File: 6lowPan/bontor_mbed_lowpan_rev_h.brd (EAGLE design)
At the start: 99.6 x 107 mm, 172 parts, among them IC1 SIM900, IC2 74HC595D, IC3 74HC595D, IC4 ADE7758RW, IC5 74HC595D, U2 W5500, X1 NX2520SA

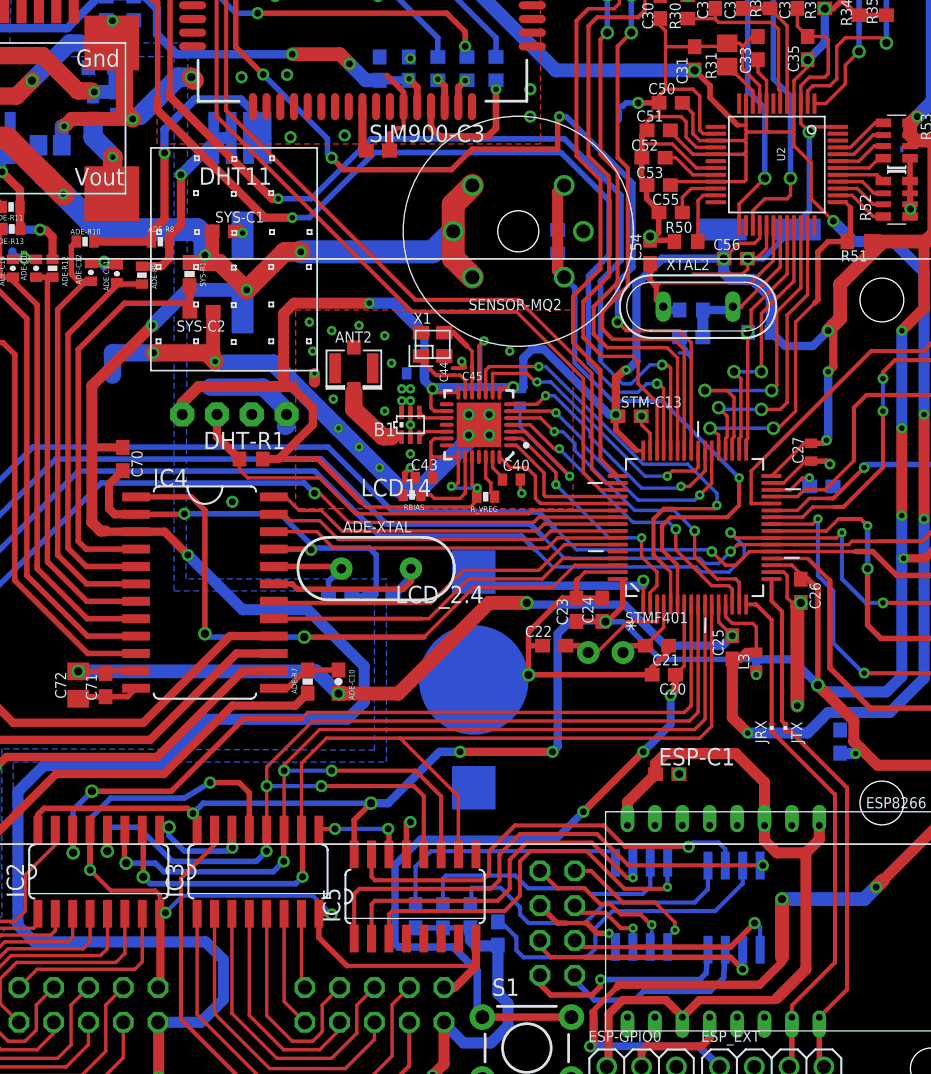
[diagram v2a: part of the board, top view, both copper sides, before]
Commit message: added on off button and remove LCD resstor
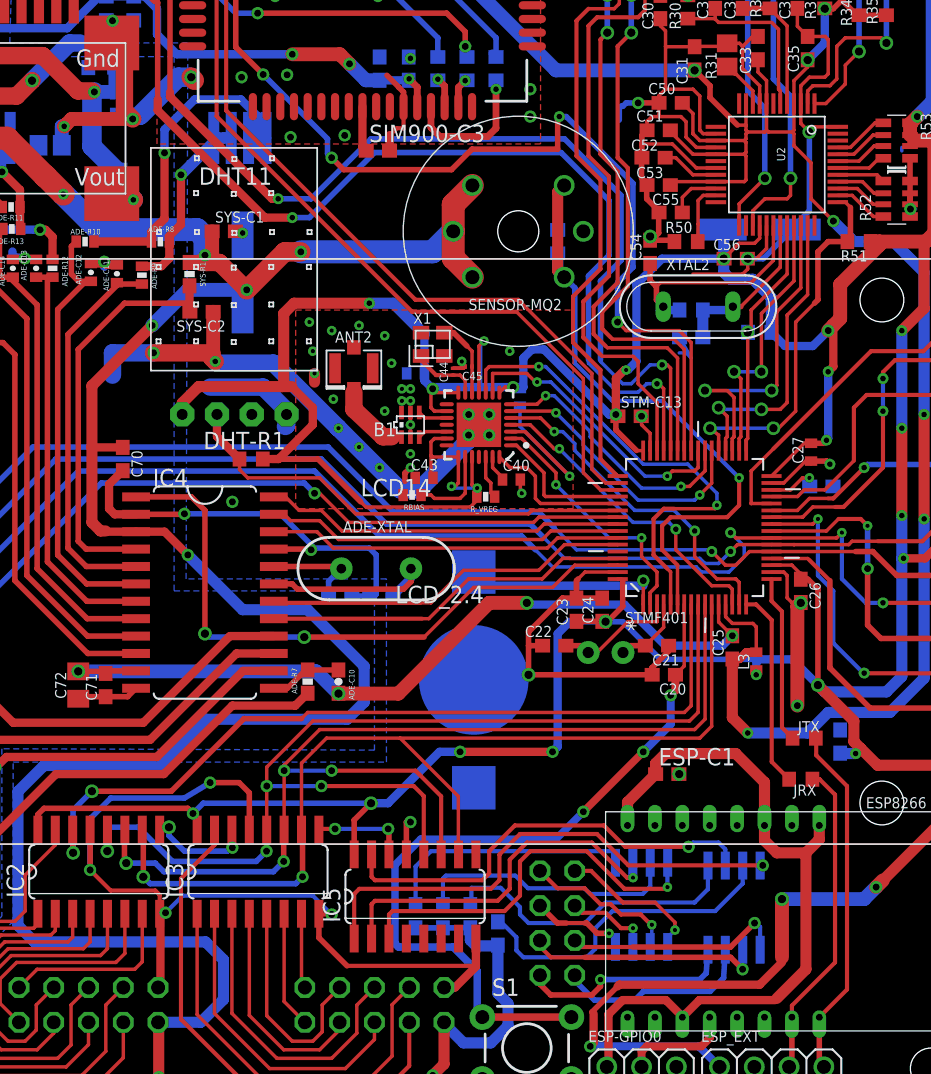
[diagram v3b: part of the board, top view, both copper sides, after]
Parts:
- JRX, JTX: device rcl:R0201 -> rcl:R0603
- PWR: device rcl:R0402 -> rcl:R0805
- moved PWR 5.89 mm to (37.3, 66.8)
- moved JRX 4.31 mm to (87.2, 23.4), turned to 180 degrees
- moved JTX 1.57 mm to (87.5, 26.4), turned to 180 degrees
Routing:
- net VDD: track 578.3 -> 584.9 mm
- net N$71: track 9.96 -> 14.5 mm
- net ESP_RX: track 27.8 -> 23.4 mm
- net DC_VOUT: track 6.23 -> 3.97 mm
- net ESP_TX: track 27.6 -> 25.9 mm
- net N$72: track 11.0 -> 12.3 mm
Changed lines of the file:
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@@
 <attribute name="VALUE" x="80.33" y="86.675" size="1.27" layer="27" rot="R180"/>
 </element>
-<element name="PWR" library="rcl" package="R0402" value="" x="35.5875" y="72.4125" smashed="yes" rot="MR270">
-<attribute name="NAME" x="36.1725" y="71.2025" size="0.6096" layer="26" rot="MR90"/>
-<attribute name="VALUE" x="37.4925" y="73.0475" size="1.27" layer="28" rot="MR270"/>
+<element name="PWR" library="rcl" package="R0805" value="" x="37.3375" y="66.7875" smashed="yes" rot="MR270">
+<attribute name="NAME" x="37.9225" y="65.5775" size="0.6096" layer="26" rot="MR90"/>
+<attribute name="VALUE" x="39.2425" y="67.4225" size="1.27" layer="28" rot="MR270"/>
 </element>
 <element name="S1" library="SparkFun-Electromechanical" package="TACTILE-PTH" value="" x="67.25" y="3.75"/>
@@
 <attribute name="VALUE" x="69.46" y="98.0975" size="1.27" layer="27" font="vector" ratio="10" rot="R270"/>
 </element>
-<element name="JRX" library="rcl" package="R0201" value="0" x="85.125" y="27.125" smashed="yes" rot="R90">
-<attribute name="NAME" x="84.74" y="25.99" size="0.8128" layer="25" rot="R90"/>
-<attribute name="VALUE" x="87.03" y="26.49" size="1.27" layer="27" rot="R90"/>
-</element>
-<element name="JTX" library="rcl" package="R0201" value="0" x="86.125" y="27.125" smashed="yes" rot="R90">
-<attribute name="NAME" x="87.365" y="25.99" size="0.8128" layer="25" rot="R90"/>
-<attribute name="VALUE" x="88.03" y="26.49" size="1.27" layer="27" rot="R90"/>
+<element name="JRX" library="rcl" package="R0603" value="0" x="87.25" y="23.375" smashed="yes" rot="R180">
+<attribute name="NAME" x="88.385" y="22.99" size="0.8128" layer="25" rot="R180"/>
+<attribute name="VALUE" x="87.885" y="25.28" size="1.27" layer="27" rot="R180"/>
+</element>
+<element name="JTX" library="rcl" package="R0603" value="0" x="87.5" y="26.375" smashed="yes" rot="R180">
+<attribute name="NAME" x="88.635" y="27.615" size="0.8128" layer="25" rot="R180"/>
+<attribute name="VALUE" x="88.135" y="28.28" size="1.27" layer="27" rot="R180"/>
 </element>
 <element name="ANT1" library="SparkFun" package="U.FL" value="U.FL" x="56.125" y="103.5" smashed="yes" rot="R270"/>
@@
 <wire x1="43.2125" y1="99.375" x2="41.825" y2="99.375" width="1.4224" layer="1"/>
 <contactref element="U$17" pad="VCC"/>
-<wire x1="35.5875" y1="73.0625" x2="35.5375" y2="73.1125" width="0.6096" layer="16"/>
 <wire x1="37.3125" y1="73.55" x2="35.675" y2="73.55" width="1.016" layer="16"/>
 <wire x1="31.9" y1="76.2" x2="27" y2="76.2" width="1.27" layer="1"/>
@@
 <via x="94.75" y="39.5" extent="1-16" drill="0.4"/>
 <wire x1="94.75" y1="39.5" x2="94.625" y2="39.5" width="0.6096" layer="16"/>
+<wire x1="37.3375" y1="67.7375" x2="35.5" y2="69.575" width="1.4224" layer="16"/>
+<wire x1="35.5" y1="69.575" x2="35.5" y2="73.375" width="1.4224" layer="16"/>
+<wire x1="35.5" y1="73.375" x2="35.675" y2="73.55" width="1.4224" layer="16"/>
 </signal>
 <signal name="SWD_NRST">
@@
 <wire x1="86.395" y1="2.375" x2="86.6" y2="2.58" width="0.4064" layer="1"/>
 <wire x1="86.6" y1="2.58" x2="86.6" y2="6" width="0.4064" layer="1"/>
-<wire x1="85.125" y1="26.87" x2="89.75" y2="22.245" width="0.3048" layer="1"/>
 <wire x1="89.75" y1="22.245" x2="89.75" y2="10" width="0.3048" layer="1"/>
+<wire x1="89.75" y1="22.245" x2="88.62" y2="23.375" width="0.3048" layer="1"/>
+<wire x1="88.62" y1="23.375" x2="88.1" y2="23.375" width="0.3048" layer="1"/>
 </signal>
 <signal name="ESP_TX">
 <contactref element="ESP" pad="TXD"/>
 <wire x1="88.6" y1="6" x2="90.625" y2="8.025" width="0.3048" layer="1"/>
-<wire x1="90.625" y1="22.75" x2="90.625" y2="8.025" width="0.3048" layer="1"/>
+<wire x1="90.625" y1="22.875" x2="90.625" y2="8.025" width="0.3048" layer="1"/>
 <contactref element="JTX" pad="1"/>
-<wire x1="90.625" y1="22.75" x2="86.505" y2="26.87" width="0.3048" layer="1"/>
-<wire x1="86.505" y1="26.87" x2="86.125" y2="26.87" width="0.3048" layer="1"/>
 <contactref element="ESP_EXT" pad="4"/>
 <wire x1="88.935" y1="2.375" x2="88.6" y2="2.71" width="0.4064" layer="1"/>
 <wire x1="88.6" y1="2.71" x2="88.6" y2="6" width="0.4064" layer="1"/>
+<wire x1="90.625" y1="22.875" x2="88.375" y2="25.125" width="0.3048" layer="1"/>
+<wire x1="88.375" y1="25.125" x2="88.375" y2="26.35" width="0.3048" layer="1"/>
+<wire x1="88.375" y1="26.35" x2="88.35" y2="26.375" width="0.3048" layer="1"/>
 </signal>
 <signal name="ESP_GPIO0">
@@
 <contactref element="PWR" pad="2"/>
 <contactref element="DCDC" pad="VOUT"/>
-<wire x1="35.5875" y1="71.7625" x2="35.5875" y2="71.0125" width="0.6096" layer="16"/>
-<wire x1="35.5875" y1="71.0125" x2="35.5875" y2="70.2375" width="1.4224" layer="16"/>
-<wire x1="35.5875" y1="70.2375" x2="37.025" y2="68.8" width="1.4224" layer="16"/>
-<via x="37.025" y="68.8" extent="1-16" drill="0.4"/>
-<wire x1="37.025" y1="68.8" x2="37.025" y2="68.775" width="1.4224" layer="1"/>
-<wire x1="37.025" y1="68.775" x2="36.95" y2="66.125" width="1.4224" layer="1"/>
+<via x="38.525" y="65.675" extent="1-16" drill="0.4"/>
+<wire x1="38.525" y1="65.675" x2="37.025" y2="66.9" width="1.4224" layer="1"/>
+<wire x1="37.025" y1="66.9" x2="36.95" y2="66.125" width="1.4224" layer="1"/>
+<wire x1="37.3375" y1="65.8375" x2="37.5" y2="65.675" width="1.4224" layer="16"/>
+<wire x1="37.5" y1="65.675" x2="38.525" y2="65.675" width="1.4224" layer="16"/>
 </signal>
 <signal name="VBAT">
@@
 <contactref element="STMF401" pad="16"/>
 <contactref element="JRX" pad="2"/>
-<wire x1="85.125" y1="27.38" x2="85.125" y2="35" width="0.3048" layer="1"/>
 <wire x1="83.9884" y1="36.1366" x2="83.2592" y2="36.1366" width="0.3048" layer="1"/>
 <wire x1="83.9884" y1="36.1366" x2="85.125" y2="35" width="0.3048" layer="1"/>
+<wire x1="86.4" y1="23.375" x2="85.125" y2="24.65" width="0.3048" layer="1"/>
+<wire x1="85.125" y1="24.65" x2="85.125" y2="35" width="0.3048" layer="1"/>
 </signal>
 <signal name="N$72">
@@
 <wire x1="85.1134" y1="37.9908" x2="85.1134" y2="36.3866" width="0.3048" layer="1"/>
 <wire x1="85.1134" y1="36.3866" x2="85.875" y2="35.625" width="0.3048" layer="1"/>
-<wire x1="85.875" y1="35.625" x2="85.875" y2="27.63" width="0.3048" layer="1"/>
-<wire x1="85.875" y1="27.63" x2="86.125" y2="27.38" width="0.3048" layer="1"/>
+<wire x1="86.65" y1="26.375" x2="85.875" y2="27.15" width="0.3048" layer="1"/>
+<wire x1="85.875" y1="27.15" x2="85.875" y2="35.625" width="0.3048" layer="1"/>
 </signal>
 <signal name="N$73">
